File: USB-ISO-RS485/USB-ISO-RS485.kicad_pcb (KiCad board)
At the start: 2 copper layers, 37 parts, among them P1 RS485 Connector, P10 TST, P11 TST, P12 TST, P13 UART Interface, P2 USB_A, P3 TST, P4 TST, P5 TST, P6 TST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

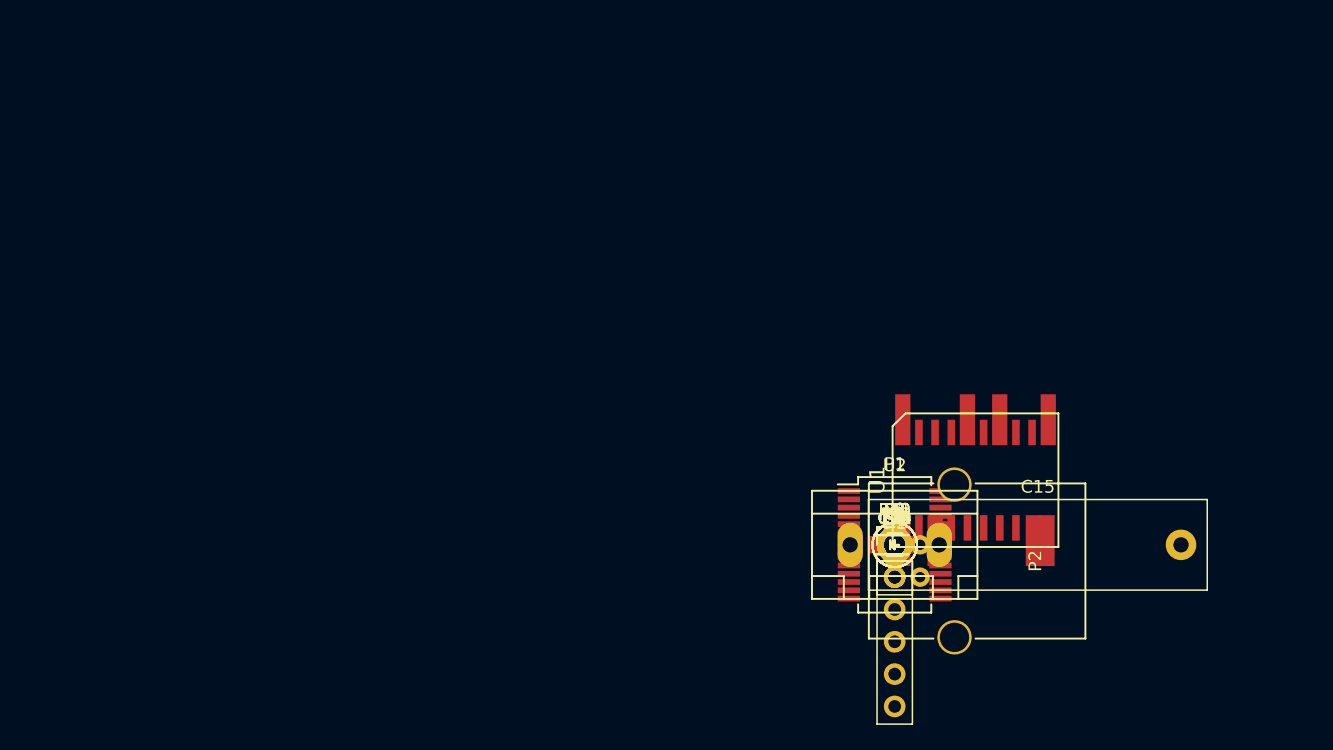
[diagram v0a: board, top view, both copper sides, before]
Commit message: broken layout - ADM2582E footprint to narrow
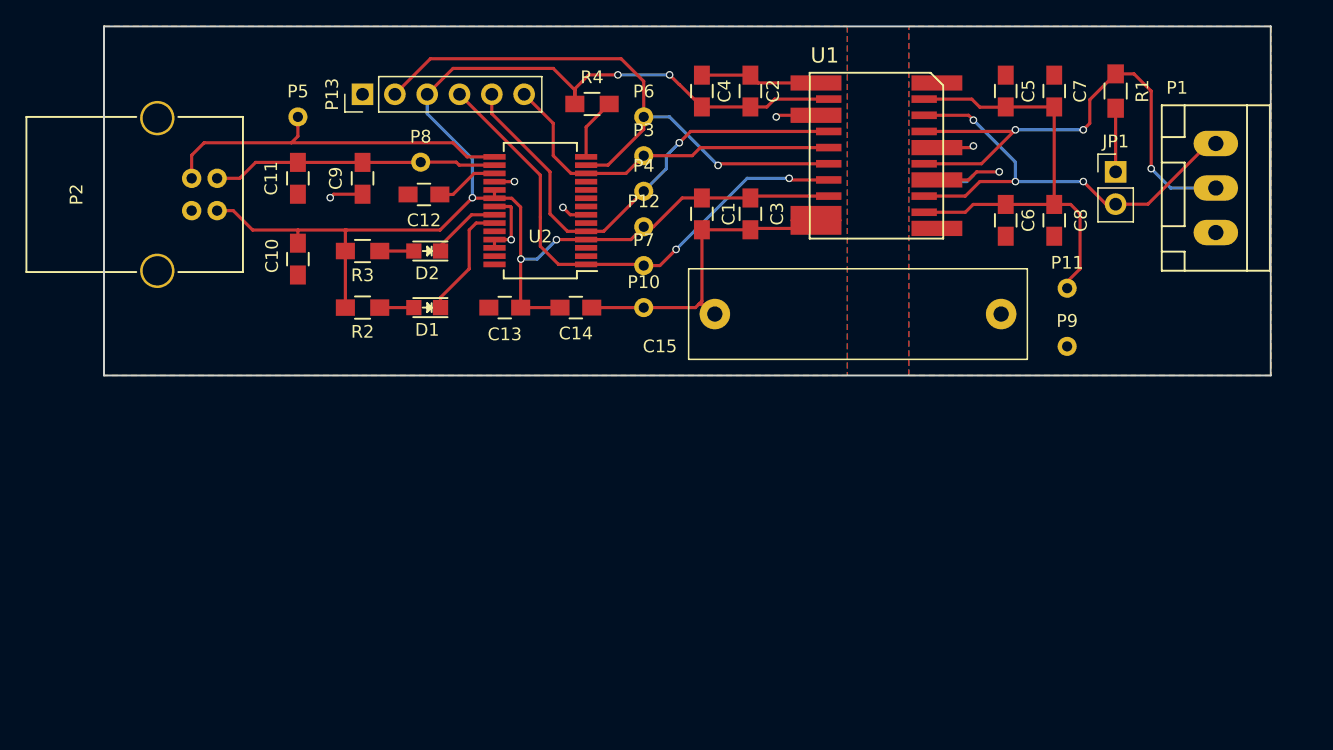
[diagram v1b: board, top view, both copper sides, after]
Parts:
- P10, P11, P12, P3, P4, P5, P6, P7, P8, P9: footprint Measurement_Points:Test_Point_Keystone_5010-5014_Multipurpose -> Measurement_Points:Measurement_Point_Round-TH_Small
- moved P2 59.4 mm to (95.2, 78.7), turned to 180 degrees
- moved P5 57.7 mm to (101.6, 71.4)
- moved C11 55.0 mm to (101.6, 76.2), turned to 90 degrees
- moved P13 54.8 mm to (106.7, 69.6), turned to 90 degrees
- moved C10 52.0 mm to (101.6, 82.5), turned to 270 degrees
- moved C9 50.8 mm to (106.7, 76.2), turned to 90 degrees
- moved P8 47.9 mm to (111.3, 74.9)
- moved R3 47.8 mm to (106.7, 81.9)
- moved C12 46.1 mm to (111.5, 77.5)
- moved R2 45.8 mm to (106.7, 86.4)
- moved D2 43.4 mm to (111.8, 81.9), turned to 180 degrees
- moved R4 42.0 mm to (124.7, 70.4)
- moved D1 41.2 mm to (111.8, 86.4), turned to 180 degrees
- moved R1 39.7 mm to (165.9, 69.3), turned to 270 degrees
- moved P6 39.0 mm to (128.8, 71.4)
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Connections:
- P13 pad 2: TxD -> DE
- P13 pad 3: DE -> +5V
- P13 pad 4: RxD -> TxD
- P13 pad 5: ~RE -> RxD
- P13 pad 6: +5V -> ~RE
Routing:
- net +5V: track 0.00 -> 117.8 mm, vias 0 -> 5
- net GND: track 0.00 -> 52.9 mm, vias 0 -> 5
- net DE: track 0.00 -> 47.1 mm, vias 0 -> 1
- net B: track 0.00 -> 41.4 mm, vias 0 -> 3
- net TxD: track 0.00 -> 41.0 mm, vias 0 -> 2
- net RxD: track 0.00 -> 37.6 mm, vias 0 -> 1
- net +3V3: track 0.00 -> 37.2 mm
- net A: track 0.00 -> 36.3 mm, vias 0 -> 3
- net ~RE: track 0.00 -> 28.8 mm
- net USBD+: track 0.00 -> 28.7 mm
- net USBD-: track 0.00 -> 22.4 mm
- net GNDA: track 0.00 -> 10.7 mm, vias 0 -> 2
- net Net-(D1-Pad1): track 0.00 -> 9.24 mm
- net Net-(D2-Pad1): track 0.00 -> 5.66 mm
- net Net-(JP1-Pad1): track 0.00 -> 5.00 mm
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- added copper zone on B.Cu, net GND
- added copper zone on F.Cu, net GND
- added copper zone on B.Cu, net GNDA
- added copper zone on F.Cu, net GNDA
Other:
- board outline added: 91.7 x 27.4 mm

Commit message: added corrected footprint, rerouted board
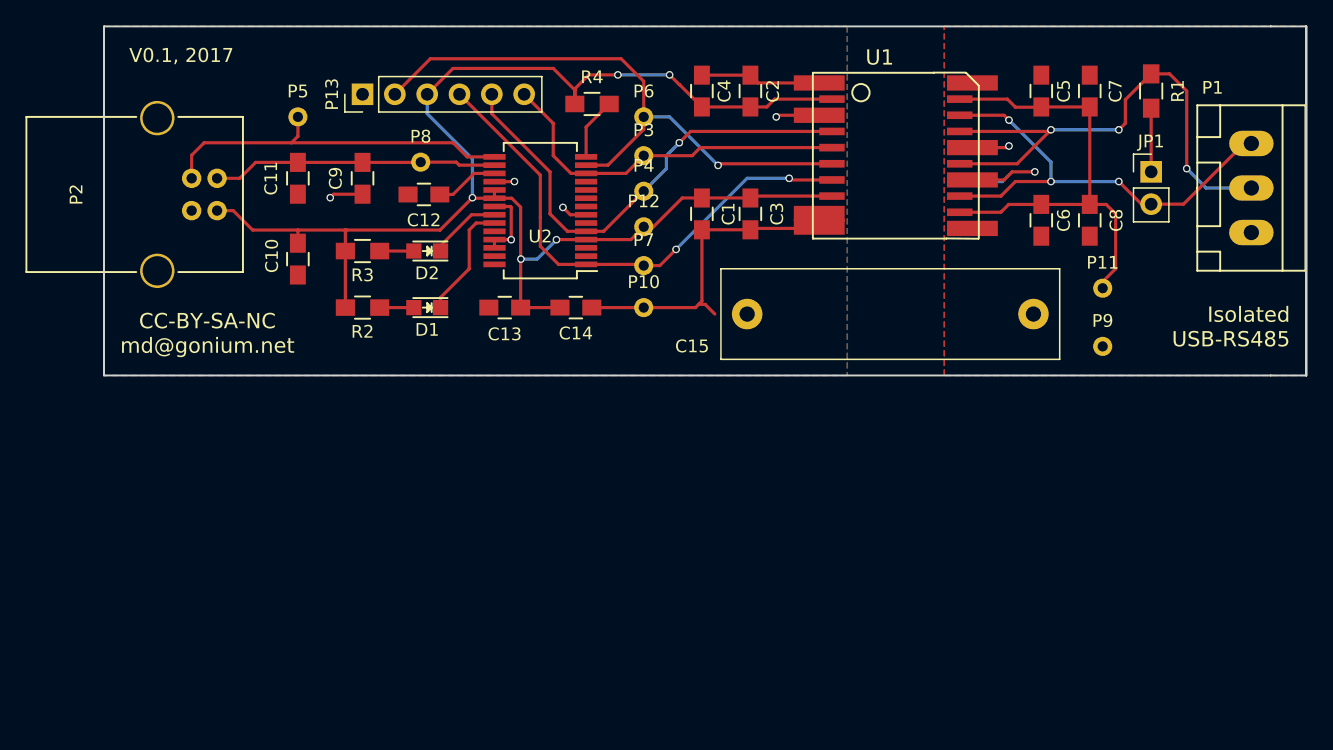
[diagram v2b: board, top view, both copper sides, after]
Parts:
- U1: footprint ADM2582E:ADM2582E-SOIC20W-Thermal -> ADM2582E:ADM2582E-SOIC20W-Thermal-Correct
- moved C5 2.79 mm to (160.0, 69.3)
- moved C6 2.79 mm to (160.0, 79.5)
- moved C7 2.79 mm to (163.8, 69.3)
- moved C8 2.79 mm to (163.8, 79.5)
- moved JP1 2.79 mm to (168.7, 75.7)
- moved P1 2.79 mm to (176.5, 77.0)
- moved P11 2.79 mm to (164.8, 84.8)
- moved P9 2.79 mm to (164.8, 89.4)
- moved R1 2.79 mm to (168.7, 69.3)
- moved C15 2.54 mm to (136.9, 86.9)
- moved U1 0.25 mm to (142.2, 68.1)
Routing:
- net GNDA: track 10.7 -> 10.1 mm
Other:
- board size 91.7 x 27.4 mm -> 94.5 x 27.4 mm
- rule trace_min: 0.2 -> 0.1
- rule via_min_size: 0.4 -> 0.2
- board text added: "CC-BY-SA-NC md@gonium.net"
- board text added: "Isolated USB-RS485"
- board text added: "V0.1, 2017"

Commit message: v0.2 board layout complete
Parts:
- removed P13: UART Interface, Pin_Headers:Pin_Header_Straight_1x06_Pitch2.54mm
- removed P4, P5, P6, P7, P8: TST, Measurement_Points:Measurement_Point_Round-TH_Small
- added C16: 100nF, Capacitors_SMD:C_0805_HandSoldering, F.Cu at (122.9, 70.4)
- added D3: P6SMB 6,8CA, ADM2582E:P6SMB6,8CA, F.Cu at (99.8, 87.6)
- added D4: P6SMB 6,8CA, ADM2582E:P6SMB6,8CA, F.Cu at (105.2, 69.8)
- added D5: P6SMB 6,8CA, ADM2582E:P6SMB6,8CA, F.Cu at (100.1, 69.8)
- added FB1: BLM21PG 600, Resistors_SMD:R_0805_HandSoldering, F.Cu at (107.2, 82.0)
- added Q1: IRLML6402, ADM2582E:IRLML6402, F.Cu at (122.7, 75.7)
- added R5: 0, Resistors_SMD:R_0805_HandSoldering, F.Cu at (95.5, 88.4)
- added R6: 100k, Resistors_SMD:R_0805_HandSoldering, F.Cu at (120.4, 80.0)
- P1: value RS485 Connector -> WAGO 233-503; footprint Connectors_WAGO:WAGO_734_3pin_Straight_RuggedPads -> ADM2582E:WAGO233-503
- R4: value 10k -> 4k7
- moved P1 20.3 mm to (156.7, 81.3), turned to 90 degrees
- moved JP1 16.6 mm to (157.7, 88.1), turned to 90 degrees
- moved P11 15.8 mm to (149.1, 85.3)
- moved P9 15.5 mm to (149.4, 88.6)
- moved C15 15.2 mm to (121.7, 87.4)
- moved C8 12.5 mm to (151.4, 80.5)
- moved P10 12.2 mm to (117.1, 82.8)
- moved C6 11.7 mm to (148.3, 80.5)
- moved C7 11.7 mm to (152.1, 70.1)
- moved P12 11.7 mm to (117.1, 80.0)
- moved C2 11.5 mm to (125.7, 70.4)
- moved C5 11.5 mm to (148.6, 70.1)
- moved R1 10.7 mm to (158.0, 69.8), turned to 0 degrees
- moved U1 10.5 mm to (131.8, 69.1)
- moved C3 8.95 mm to (128.3, 80.0)
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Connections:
- C1 pad 1: +5V -> 5V-Switched
- C10 pad 1: +5V -> Net-(C10-Pad1)
- C11 pad 1: GND -> USBD+
- C11 pad 2: USBD- -> GND
- C2 pad 1: +5V -> 5V-Switched
- C3 pad 1: +5V -> 5V-Switched
- C4 pad 1: +5V -> 5V-Switched
- C9 pad 1: GND -> USBD-
- C9 pad 2: USBD- -> GND
- P2 pad 1: +5V -> Net-(C10-Pad1)
- P2 pad 5: GND -> Shield
- P3 pad 1: ~RE -> 5V-Switched
- R4 pad 1: +5V -> Net-(R4-Pad1)
- R4 pad 2: Net-(R4-Pad2) -> Net-(C16-Pad2)
- U1 pad 2: +5V -> 5V-Switched
- U1 pad 8: +5V -> 5V-Switched
- U2 pad 14: Net-(R4-Pad2) -> Net-(R4-Pad1)
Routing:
- net GNDA: track 10.1 -> 75.5 mm, vias 2 -> 21
- net +5V: track 117.8 -> 58.2 mm, vias 5 -> 2
- net Shield: track 0.00 -> 42.8 mm, vias 0 -> 13
- net (no net): track 1.73 -> 43.3 mm, vias 0 -> 19
- net 5V-Switched: track 0.00 -> 30.8 mm
- net GND: track 52.9 -> 25.4 mm, vias 5 -> 3
- net DE: track 47.1 -> 19.8 mm, vias 1 -> 2
- net TxD: track 41.0 -> 15.9 mm
- net Net-(C10-Pad1): track 0.00 -> 22.0 mm
- net RxD: track 37.6 -> 18.9 mm, vias 1 -> 2
- net Net-(JP1-Pad1): track 5.00 -> 19.0 mm
- net Net-(D2-Pad1): track 5.66 -> 16.9 mm, vias 0 -> 2
- net A: track 36.3 -> 47.3 mm, vias 3 -> 2
- net Net-(C16-Pad2): track 0.00 -> 9.61 mm
- net Net-(R4-Pad1): track 0.00 -> 7.27 mm
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- added copper zone on B.Cu, net Shield
- added copper zone on F.Cu, net Shield
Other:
- board size 94.5 x 27.4 mm -> 78.2 x 25.1 mm
- net class Data added: clearance 0.2, trace_width 0.2, via_dia 0.6, via_drill 0.4
- net class Default: trace_width 0.25 -> 0.35
- board text added: "A|B|G"
- board text added: "Connection: A, B and GND Terminator: 120 Ohm"
- board text added: "Isolated USB-RS485 Adaptor v0.2, 2017 CC-BY-NC-SA md@gonium.net"
- board text added: "Terminator"
- board text added: "USB- ISO- RS485"
- board text removed: "CC-BY-SA-NC md@gonium.net"
- board text removed: "Isolated USB-RS485"
- board text removed: "V0.1, 2017"

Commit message: working on v0.2
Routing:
- net GNDA: track 75.5 -> 13.3 mm, vias 21 -> 3
- net (no net): track 43.3 -> 74.4 mm, vias 19 -> 25
